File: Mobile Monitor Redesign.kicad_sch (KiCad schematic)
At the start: 48 parts, among them J1 Conn_01x02_Pin, J2 Conn_01x08_Pin, J3 Conn_01x08_Pin, J5 Conn_02x03_Odd_Even, J6 Micro_SD_Card_Det1, J7 Conn_01x05_Pin, J8 Conn_01x06_Socket, Q1 2N7002, Q2 AO3401A, Q3 BSS138, Q4 BSS138, U1 ATmega2560-16A, U11 TPL5010, U2 DS3232M, U3 AP2112K-3.3, U4 L80-R, U7 CH340C, Y2 Crystal

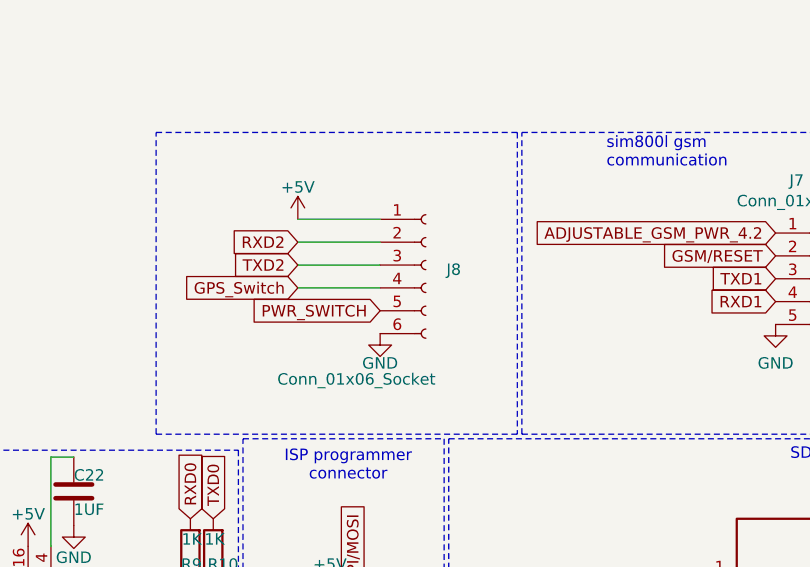
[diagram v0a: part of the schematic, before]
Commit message: added another pin for power connection
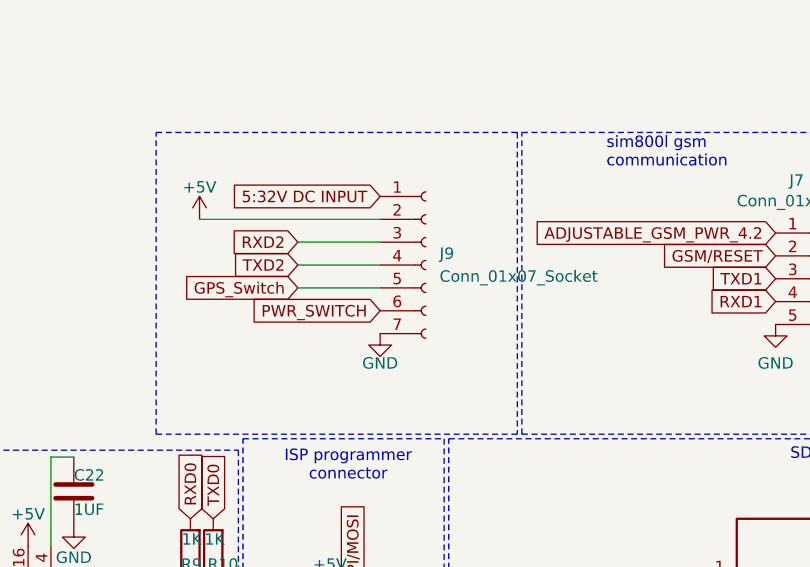
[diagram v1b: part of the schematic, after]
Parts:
- removed J8: Conn_01x06_Socket, Connector_PinHeader_2.54mm:PinHeader_1x06_P2.54mm_Horizontal, symbol Connector:Conn_01x06_Socket
- added J9: Conn_01x07_Socket, Connector_PinHeader_2.54mm:PinHeader_1x07_P2.54mm_Horizontal, symbol Connector:Conn_01x07_Socket
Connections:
- net +5V: now also J9.2 (Pin_2)
- net GND: now also J9.7 (Pin_7)
- net GPS_Switch: now also J9.5 (Pin_5)
- net PWR_SWITCH: now also J9.6 (Pin_6)
- net RXD2: now also J9.3 (Pin_3)
- net TXD2: now also J9.4 (Pin_4)
- new net 5:32V DC INPUT: J9.1 (Pin_1)
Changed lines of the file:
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@@
 	(wire
 		(pts
-			(xy 159.766 44.196) (xy 150.622 44.196)
+			(xy 159.766 44.196) (xy 139.7 44.196)
 		)
 		(stroke
@@
 		)
 	)
+	(global_label "5:32V DC INPUT"
+		(shape input)
+		(at 159.766 41.656 180)
+		(fields_autoplaced yes)
+		(effects
+			(font
+				(size 1.27 1.27)
+			)
+			(justify right)
+		)
+		(property "Intersheetrefs" "${INTERSHEET_REFS}"
+			(at 141.4803 41.656 0)
+			(effects
+				(font
+					(size 1.27 1.27)
+				)
+				(justify right)
+				(hide yes)
+			)
+		)
+	)
 	(global_label "gps_tx"
 		(shape input)
@@
 	)
 	(symbol
+		(lib_id "Connector:Conn_01x07_Socket")
+		(at 164.846 49.276 0)
+		(unit 1)
+		(exclude_from_sim no)
+		(in_bom yes)
+		(on_board yes)
+		(dnp no)
+		(fields_autoplaced yes)
+		(property "Reference" "J9"
+			(at 166.37 48.0059 0)
+			(effects
+				(font
+					(size 1.27 1.27)
+				)
+				(justify left)
+			)
+		)
+		(property "Value" "Conn_01x07_Socket"
+			(at 166.37 50.5459 0)
+			(effects
+				(font
+					(size 1.27 1.27)
+				)
+				(justify left)
+			)
+		)
+		(property "Footprint" "Connector_PinHeader_2.54mm:PinHeader_1x07_P2.54mm_Horizontal"
+			(at 164.846 49.276 0)
+			(effects
+				(font
+					(size 1.27 1.27)
+				)
+				(hide yes)
+			)
+		)
+		(property "Datasheet" "~"
+			(at 164.846 49.276 0)
+			(effects
+				(font
+					(size 1.27 1.27)
+				)
+				(hide yes)
+			)
+		)
+		(property "Description" "Generic connector, single row, 01x07, script generated"
+			(at 164.846 49.276 0)
+			(effects
+				(font
+					(size 1.27 1.27)
+				)
+				(hide yes)
+			)
+		)
+		(pin "1"
+		)
+		(pin "2"
+		)
+		(pin "3"
+		)
+		(pin "4"
+		)
+		(pin "5"
+		)
+		(pin "6"
+		)
+		(pin "7"
+		)
+		(instances
+			(project ""
+				(path "/b7045867-46a9-42d4-b526-22005757f9bb"
+					(reference "J9")
+					(unit 1)
+				)
+			)
+		)
+	)
+	(symbol
 		(lib_id "Device:R")
 		(at 205.232 156.972 180)
@@
 	)
 	(symbol
-		(lib_id "Connector:Conn_01x06_Socket")
-		(at 164.846 49.276 0)
-		(unit 1)
-		(exclude_from_sim no)
-		(in_bom yes)
-		(on_board yes)
-		(dnp no)
-		(property "Reference" "J8"
-			(at 167.132 49.784 0)
-			(effects
-				(font
-					(size 1.27 1.27)
-				)
-				(justify left)
-			)
-		)
-		(property "Value" "Conn_01x06_Socket"
-			(at 148.336 61.976 0)
-			(effects
-				(font
-					(size 1.27 1.27)
-				)
-				(justify left)
-			)
-		)
-		(property "Footprint" "Connector_PinHeader_2.54mm:PinHeader_1x06_P2.54mm_Horizontal"
-			(at 164.846 49.276 0)
-			(effects
-				(font
-					(size 1.27 1.27)
-				)
-				(hide yes)
-			)
-		)
-		(property "Datasheet" "~"
-			(at 164.846 49.276 0)
-			(effects
-				(font
-					(size 1.27 1.27)
-				)
-				(hide yes)
-			)
-		)
-		(property "Description" "Generic connector, single row, 01x06, script generated"
-			(at 164.846 49.276 0)
-			(effects
-				(font
-					(size 1.27 1.27)
-				)
-				(hide yes)
-			)
-		)
-		(pin "1"
-		)
-		(pin "6"
-		)
-		(pin "3"
-		)
-		(pin "2"
-		)
-		(pin "4"
-		)
-		(pin "5"
-		)
-		(instances
-			(project ""
-				(path "/b7045867-46a9-42d4-b526-22005757f9bb"
-					(reference "J8")
-					(unit 1)
-				)
-			)
-		)
-	)
-	(symbol
 		(lib_id "power:GND")
 		(at 225.552 121.158 270)
@@
 	(symbol
 		(lib_id "power:+5V")
-		(at 150.622 44.196 0)
+		(at 139.7 44.196 0)
 		(unit 1)
 		(exclude_from_sim no)
@@
 		(dnp no)
 		(property "Reference" "#PWR085"
-			(at 150.622 48.006 0)
+			(at 139.7 48.006 0)
 			(effects
 				(font
@@
 		)
 		(property "Value" "+5V"
-			(at 150.622 40.64 0)
+			(at 139.7 40.64 0)
 			(effects
 				(font
@@
 		)
 		(property "Footprint" ""
-			(at 150.622 44.196 0)
+			(at 139.7 44.196 0)
 			(effects
 				(font
@@
 		)
 		(property "Datasheet" ""
-			(at 150.622 44.196 0)
+			(at 139.7 44.196 0)
 			(effects
 				(font
@@
 		)
 		(property "Description" ""
-			(at 150.622 44.196 0)
+			(at 139.7 44.196 0)
 			(effects
 				(font

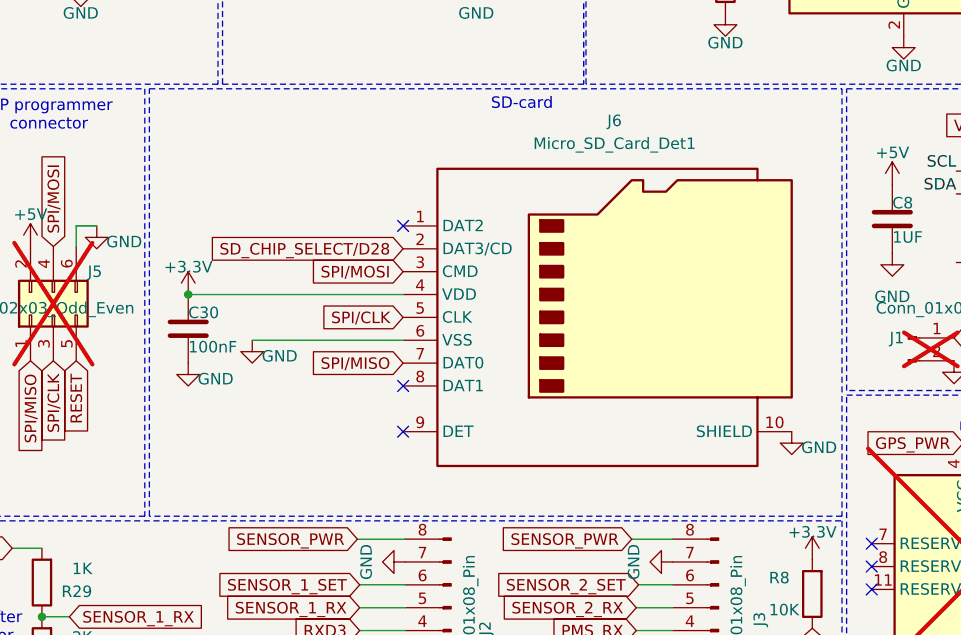
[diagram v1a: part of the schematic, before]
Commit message: removed redundant SD-card schematic on base PCB
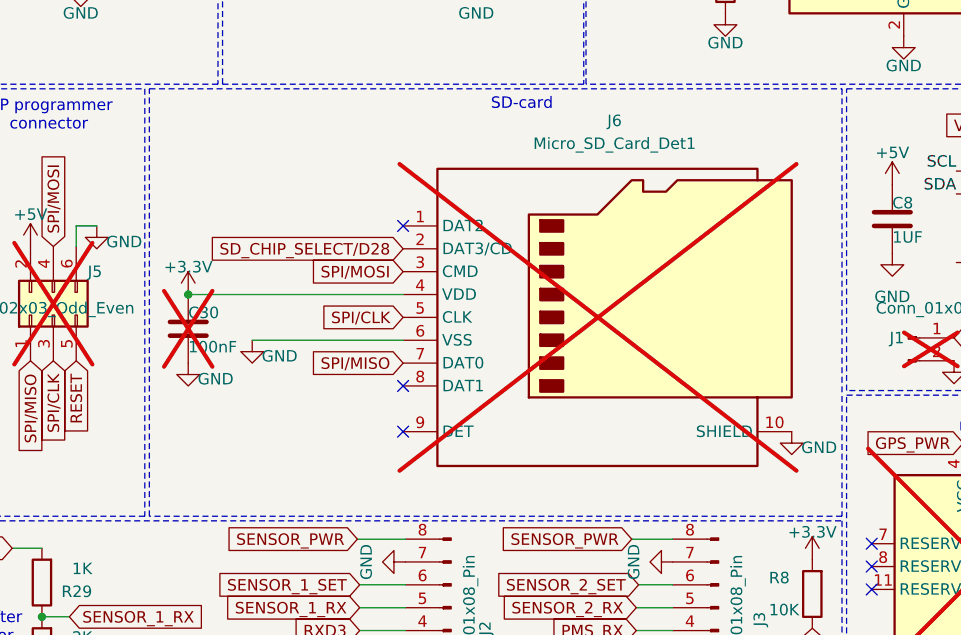
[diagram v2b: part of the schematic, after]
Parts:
- C30, J6: now not fitted; now left out of the parts list
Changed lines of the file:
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@@
 		(at 171.704 95.25 0)
 		(unit 1)
-		(exclude_from_sim no)
-		(in_bom yes)
-		(on_board yes)
-		(dnp no)
+		(exclude_from_sim yes)
+		(in_bom no)
+		(on_board no)
+		(dnp yes)
 		(property "Reference" "C30"
 			(at 171.704 93.472 0)
@@
 		(at 218.44 93.98 0)
 		(unit 1)
-		(exclude_from_sim no)
-		(in_bom yes)
-		(on_board yes)
-		(dnp no)
+		(exclude_from_sim yes)
+		(in_bom no)
+		(on_board no)
+		(dnp yes)
 		(fields_autoplaced yes)
 		(property "Reference" "J6"

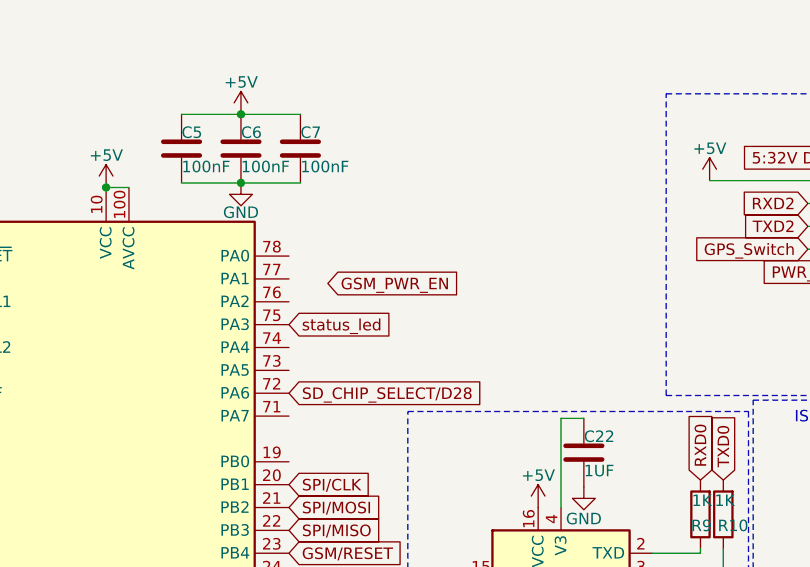
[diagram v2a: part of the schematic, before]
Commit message: recheked gps serial pin mappings
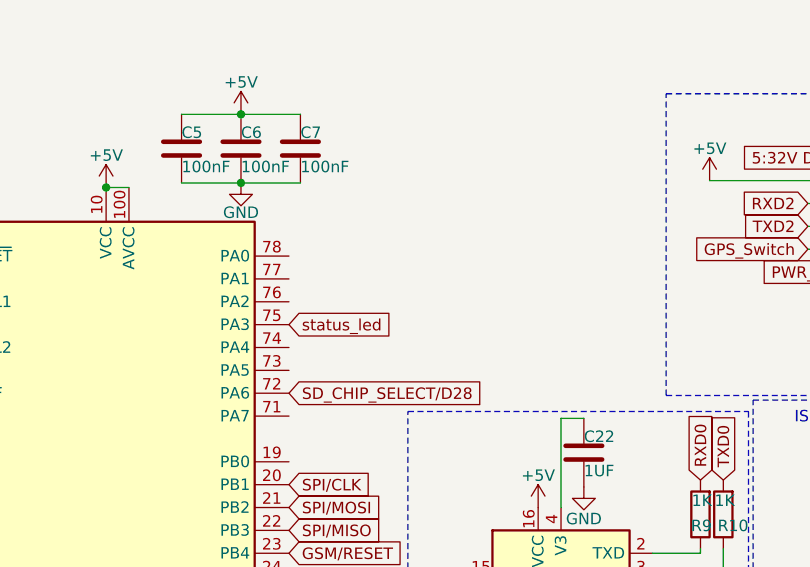
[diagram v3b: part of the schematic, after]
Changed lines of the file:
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@@
-		)
-	)
-	(global_label "GSM_PWR_EN"
-		(shape input)
-		(at 97.282 55.626 0)
-		(fields_autoplaced yes)
-		(effects
-			(font
-				(size 1.27 1.27)
-			)
-			(justify left)
-		)
-		(property "Intersheetrefs" "${INTERSHEET_REFS}"
-			(at 112.6042 55.626 0)
-			(effects
-				(font
-					(size 1.27 1.27)
-				)
-				(justify left)
-				(hide yes)
-			)
 		)
 	)
